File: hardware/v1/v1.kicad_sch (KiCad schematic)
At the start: 70 parts, among them J1 AUDIO IN, J2 MIDI OUT, J3 MIDI IN, J4 MIDI THRU, J5 OUTPUT R, J6 OUTPUT L - MONO, J7 EXP 2, J8 EXP 1, J9 Conn_01x02_Female, SW1 RotaryEncoder_Switch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

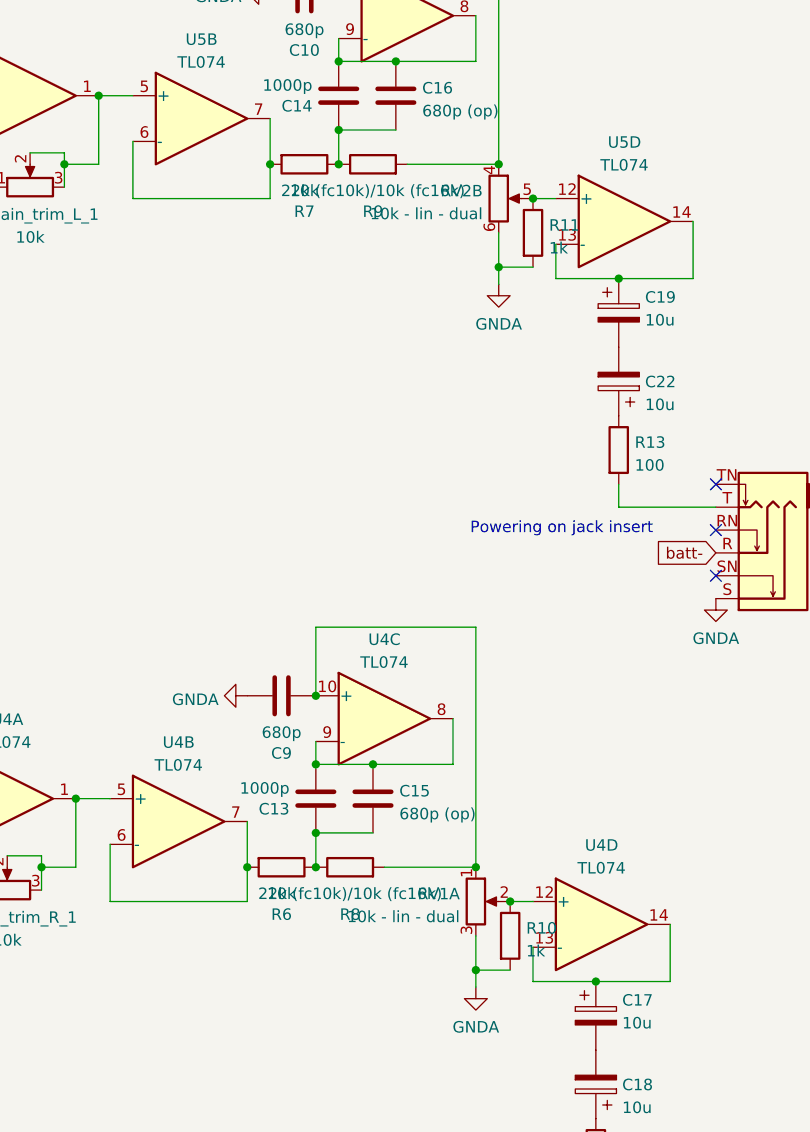
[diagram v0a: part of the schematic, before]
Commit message: Added DIN5 Midi component
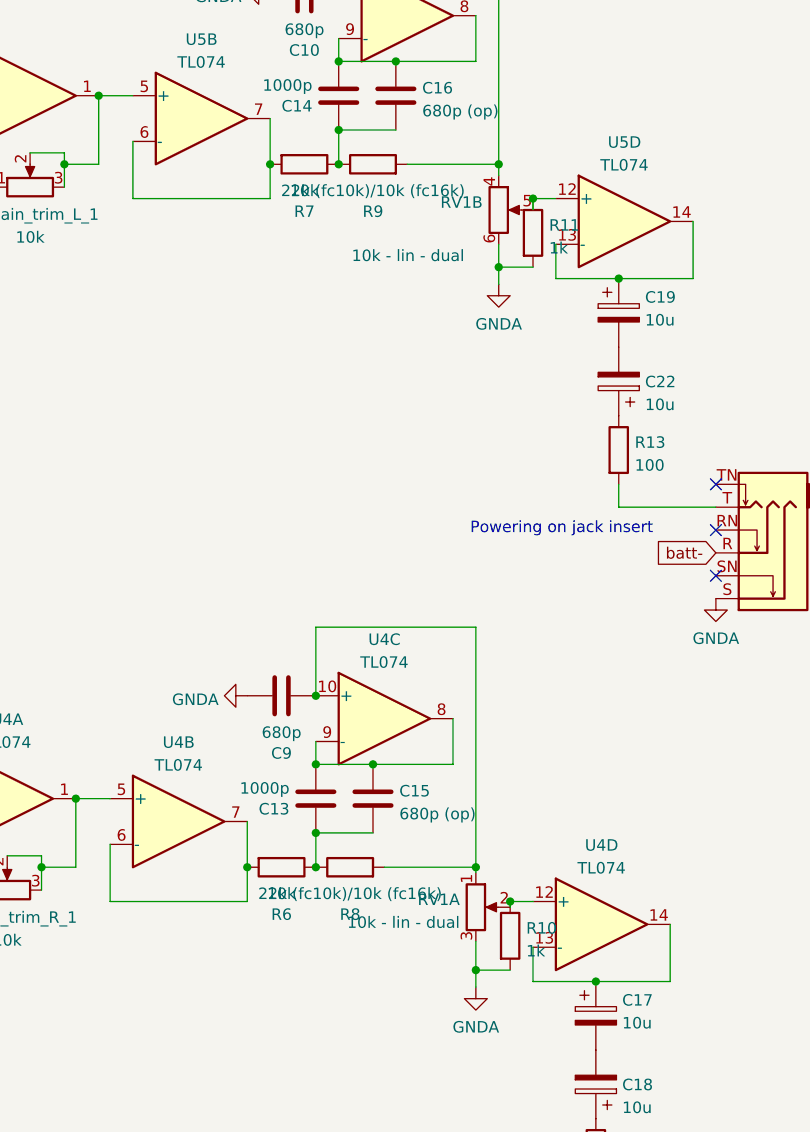
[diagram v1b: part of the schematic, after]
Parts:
- J2, J3, J4: footprint (none) -> MIDI_DIN5:DS-5 MIDI
- renumbered RV2 to RV1
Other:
- moved on the sheet: RV1A, RV1B
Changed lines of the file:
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@@
     (stroke (width 0) (type default) (color 0 0 0 0))
   )
+  (wire (pts (xy 441.96 125.73) (xy 441.96 125.095))
+    (stroke (width 0) (type default) (color 0 0 0 0))
+  )
   (wire (pts (xy 58.42 36.83) (xy 58.42 82.55))
     (stroke (width 0) (type default) (color 0 0 0 0))
@@
     (stroke (width 0) (type default) (color 0 0 0 0))
   )
+  (wire (pts (xy 445.77 129.54) (xy 445.77 128.905))
+    (stroke (width 0) (type default) (color 0 0 0 0))
+  )
   (wire (pts (xy 424.18 111.125) (xy 424.18 113.665))
     (stroke (width 0) (type default) (color 0 0 0 0))
@@
     (stroke (width 0) (type default) (color 0 0 0 0))
   )
-  (wire (pts (xy 441.96 136.525) (xy 441.96 132.715))
+  (wire (pts (xy 441.96 136.525) (xy 441.96 133.35))
     (stroke (width 0) (type default) (color 0 0 0 0))
   )
@@
     (stroke (width 0) (type default) (color 0 0 0 0))
   )
+  (wire (pts (xy 448.31 52.07) (xy 448.31 50.8))
+    (stroke (width 0) (type default) (color 0 0 0 0))
+  )
   (wire (pts (xy 444.5 60.325) (xy 444.5 58.42))
     (stroke (width 0) (type default) (color 0 0 0 0))
@@
     (stroke (width 0) (type default) (color 0 0 0 0))
   )
+  (wire (pts (xy 444.5 48.26) (xy 444.5 46.99))
+    (stroke (width 0) (type default) (color 0 0 0 0))
+  )
   (wire (pts (xy 457.835 82.55) (xy 457.835 85.09))
     (stroke (width 0) (type default) (color 0 0 0 0))
@@
     (stroke (width 0) (type default) (color 0 0 0 0))
   )
-  (wire (pts (xy 444.5 58.42) (xy 444.5 54.61))
+  (wire (pts (xy 444.5 58.42) (xy 444.5 55.88))
     (stroke (width 0) (type default) (color 0 0 0 0))
   )
@@
     (pin "4")
   )
-  (symbol (lib_id "Device:R_Potentiometer_Dual_Separate") (at 441.96 128.905 0) (unit 1)
+  (symbol (lib_id "Device:R_Potentiometer_Dual_Separate") (at 441.96 129.54 0) (unit 1)
     (in_bom yes) (on_board yes) (fields_autoplaced)
-    (property "Reference" "RV1" (id 0) (at 440.182 128.0703 0)
+    (property "Reference" "RV1" (id 0) (at 440.182 128.7053 0)
       (effects (font (size 1.27 1.27)) (justify right))
     )
-    (property "Value" "10k - lin - dual" (id 1) (at 440.182 130.6072 0)
+    (property "Value" "10k - lin - dual" (id 1) (at 440.182 131.2422 0)
       (effects (font (size 1.27 1.27)) (justify right))
     )
-    (property "Footprint" "" (id 2) (at 441.96 128.905 0)
+    (property "Footprint" "" (id 2) (at 441.96 129.54 0)
       (effects (font (size 1.27 1.27)) hide)
     )
-    (property "Datasheet" "~" (id 3) (at 441.96 128.905 0)
+    (property "Datasheet" "~" (id 3) (at 441.96 129.54 0)
       (effects (font (size 1.27 1.27)) hide)
     )
@@
     (property "Reference" "J4" (id 0) (at 263.5251 123.3002 0))
     (property "Value" "MIDI THRU" (id 1) (at 263.5251 125.8371 0))
-    (property "Footprint" "" (id 2) (at 263.525 132.08 0)
+    (property "Footprint" "MIDI_DIN5:DS-5 MIDI" (id 2) (at 263.525 132.08 0)
       (effects (font (size 1.27 1.27)) hide)
     )
@@
       (effects (font (size 1.27 1.27)) (justify right))
     )
-    (property "Footprint" "" (id 2) (at 243.205 132.715 0)
+    (property "Footprint" "MIDI_DIN5:DS-5 MIDI" (id 2) (at 243.205 132.715 0)
       (effects (font (size 1.27 1.27)) hide)
     )
@@
     (property "Reference" "J2" (id 0) (at 167.0051 124.5702 0))
     (property "Value" "MIDI OUT" (id 1) (at 167.0051 127.1071 0))
-    (property "Footprint" "" (id 2) (at 167.005 133.35 0)
+    (property "Footprint" "MIDI_DIN5:DS-5 MIDI" (id 2) (at 167.005 133.35 0)
       (effects (font (size 1.27 1.27)) hide)
     )
@@
     (pin "4")
   )
-  (symbol (lib_id "Device:R_Potentiometer_Dual_Separate") (at 444.5 50.8 0) (unit 2)
-    (in_bom yes) (on_board yes) (fields_autoplaced)
-    (property "Reference" "RV2" (id 0) (at 442.722 49.9653 0)
+  (symbol (lib_id "Device:R_Potentiometer_Dual_Separate") (at 444.5 52.07 0) (unit 2)
+    (in_bom yes) (on_board yes)
+    (property "Reference" "RV1" (id 0) (at 442.722 51.2353 0)
       (effects (font (size 1.27 1.27)) (justify right))
     )
-    (property "Value" "10k - lin - dual" (id 1) (at 442.722 52.5022 0)
+    (property "Value" "10k - lin - dual" (id 1) (at 440.69 57.15 0)
       (effects (font (size 1.27 1.27)) (justify right))
     )
-    (property "Footprint" "" (id 2) (at 444.5 50.8 0)
+    (property "Footprint" "" (id 2) (at 444.5 52.07 0)
       (effects (font (size 1.27 1.27)) hide)
     )
-    (property "Datasheet" "~" (id 3) (at 444.5 50.8 0)
+    (property "Datasheet" "~" (id 3) (at 444.5 52.07 0)
       (effects (font (size 1.27 1.27)) hide)
     )
@@
     )
     (path "/be3f2217-99de-4549-8d21-5a87292252e5"
-      (reference "J2") (unit 1) (value "MIDI OUT") (footprint "")
+      (reference "J2") (unit 1) (value "MIDI OUT") (footprint "MIDI_DIN5:DS-5 MIDI")
     )
     (path "/b1c96566-7940-49f4-a60d-f8a08bd036b1"
-      (reference "J3") (unit 1) (value "MIDI IN") (footprint "")
+      (reference "J3") (unit 1) (value "MIDI IN") (footprint "MIDI_DIN5:DS-5 MIDI")
     )
     (path "/49f76ca1-b75f-49b9-80bf-0c4c4ec1f0ea"
-      (reference "J4") (unit 1) (value "MIDI THRU") (footprint "")
+      (reference "J4") (unit 1) (value "MIDI THRU") (footprint "MIDI_DIN5:DS-5 MIDI")
     )
     (path "/eb1dfd55-7b3f-4e09-9fb1-847ee4ae89e1"
@@
     )
     (path "/c0f91244-7785-4f67-800f-3775e839ff20"
-      (reference "RV2") (unit 2) (value "10k - lin - dual") (footprint "")
+      (reference "RV1") (unit 2) (value "10k - lin - dual") (footprint "")
     )
     (path "/d7195655-bc8b-42c6-9265-3feac398262b"

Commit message: Added stamp dual pot
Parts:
- RV1: footprint (none) -> dual_pot:Dual Pot RK1114GH
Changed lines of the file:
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@@
       (effects (font (size 1.27 1.27)) (justify right))
     )
-    (property "Footprint" "" (id 2) (at 441.96 129.54 0)
+    (property "Footprint" "dual_pot:Dual Pot RK1114GH" (id 2) (at 441.96 129.54 0)
       (effects (font (size 1.27 1.27)) hide)
     )
@@
       (effects (font (size 1.27 1.27)) (justify right))
     )
-    (property "Footprint" "" (id 2) (at 444.5 52.07 0)
+    (property "Footprint" "dual_pot:Dual Pot RK1114GH" (id 2) (at 444.5 52.07 0)
       (effects (font (size 1.27 1.27)) hide)
     )
@@
     )
     (path "/1dbdedeb-a12d-4a03-88a7-8dc9f8b82f58"
-      (reference "RV1") (unit 1) (value "10k - lin - dual") (footprint "")
+      (reference "RV1") (unit 1) (value "10k - lin - dual") (footprint "dual_pot:Dual Pot RK1114GH")
     )
     (path "/c0f91244-7785-4f67-800f-3775e839ff20"
-      (reference "RV1") (unit 2) (value "10k - lin - dual") (footprint "")
+      (reference "RV1") (unit 2) (value "10k - lin - dual") (footprint "dual_pot:Dual Pot RK1114GH")
     )
     (path "/d7195655-bc8b-42c6-9265-3feac398262b"

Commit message: Added screen stamp
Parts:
- U3: footprint (none) -> TFT_Screens:TFT_2.4
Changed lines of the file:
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@@
     (property "Reference" "U3" (id 0) (at 178.435 66.201 0))
     (property "Value" "2.4inches" (id 1) (at 178.435 68.7379 0))
-    (property "Footprint" "" (id 2) (at 180.975 82.55 0)
+    (property "Footprint" "TFT_Screens:TFT_2.4" (id 2) (at 180.975 82.55 0)
       (effects (font (size 1.27 1.27)) hide)
     )
@@
     )
     (path "/bc33b228-85e6-4d5d-99b9-88d2a0d93ad5"
-      (reference "U3") (unit 1) (value "2.4inches") (footprint "")
+      (reference "U3") (unit 1) (value "2.4inches") (footprint "TFT_Screens:TFT_2.4")
     )
     (path "/4e48de9c-53a5-47eb-ae60-7f5ccb2d118e"

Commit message: started pcb
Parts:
- U1: footprint Housings_SOIC:SOIC-8_3.9x4.9mm_Pitch1.27mm -> Package_SO:SOP-8_3.9x4.9mm_P1.27mm
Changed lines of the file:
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@@
     (property "Reference" "U1" (id 0) (at 83.82 26.7802 0))
     (property "Value" "PT8211-pt8211" (id 1) (at 83.82 29.3171 0))
-    (property "Footprint" "Housings_SOIC:SOIC-8_3.9x4.9mm_Pitch1.27mm" (id 2) (at 83.82 39.37 0)
+    (property "Footprint" "Package_SO:SOP-8_3.9x4.9mm_P1.27mm" (id 2) (at 83.82 39.37 0)
       (effects (font (size 1.27 1.27) italic) hide)
     )
@@
     )
     (path "/55be732d-d054-4d1b-b915-371f3d6eb5d0"
-      (reference "U1") (unit 1) (value "PT8211-pt8211") (footprint "Housings_SOIC:SOIC-8_3.9x4.9mm_Pitch1.27mm")
+      (reference "U1") (unit 1) (value "PT8211-pt8211") (footprint "Package_SO:SOP-8_3.9x4.9mm_P1.27mm")
     )
     (path "/98f5bc82-3b1e-4f7c-9aea-552da5d9b877"

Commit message: started PCB
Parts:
- J9: footprint Connector_JST:JST_XH_B2B-XH-AM_1x02_P2.50mm_Vertical -> Connector_JST:JST_XH_B2B-XH-A_1x02_P2.50mm_Vertical
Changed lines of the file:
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@@
       (effects (font (size 1.27 1.27)) (justify left))
     )
-    (property "Footprint" "Connector_JST:JST_XH_B2B-XH-AM_1x02_P2.50mm_Vertical" (id 2) (at 249.555 26.035 0)
+    (property "Footprint" "Connector_JST:JST_XH_B2B-XH-A_1x02_P2.50mm_Vertical" (id 2) (at 249.555 26.035 0)
       (effects (font (size 1.27 1.27)) hide)
     )
@@
     )
     (path "/3ed761fc-73b0-4fad-9c40-d3c2aa5128e2"
-      (reference "J9") (unit 1) (value "Conn_01x02_Female") (footprint "Connector_JST:JST_XH_B2B-XH-AM_1x02_P2.50mm_Vertical")
+      (reference "J9") (unit 1) (value "Conn_01x02_Female") (footprint "Connector_JST:JST_XH_B2B-XH-A_1x02_P2.50mm_Vertical")
     )
     (path "/7aa8ebeb-8bea-4614-8ec6-7c790f165918"

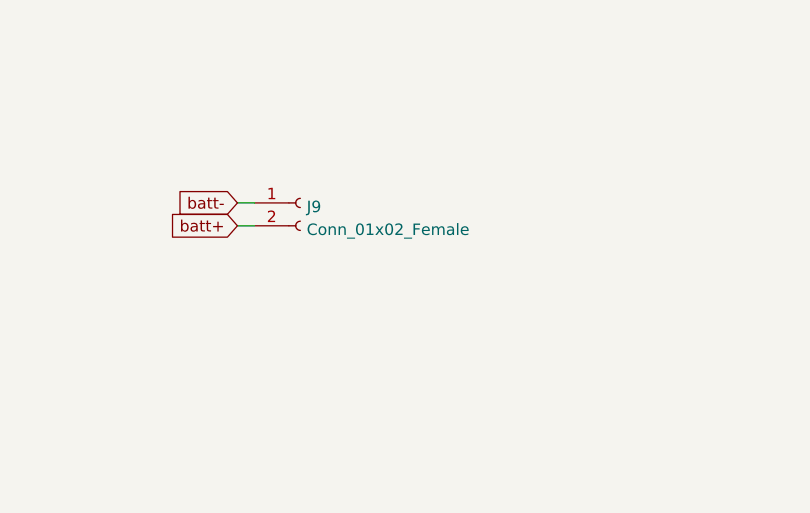
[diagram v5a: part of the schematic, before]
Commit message: Continued PCB placing
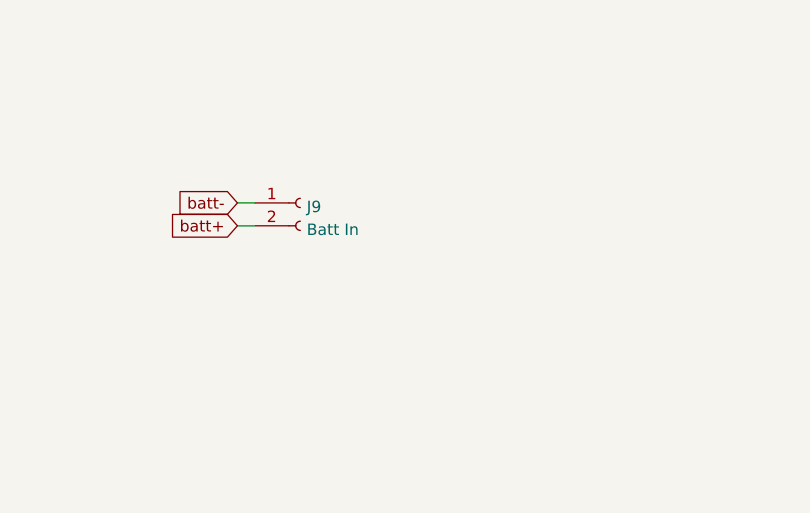
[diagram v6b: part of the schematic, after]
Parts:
- J9: value Conn_01x02_Female -> Batt In
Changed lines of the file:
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@@
       (effects (font (size 1.27 1.27)) (justify left))
     )
-    (property "Value" "Conn_01x02_Female" (id 1) (at 250.2662 29.0072 0)
+    (property "Value" "Batt In" (id 1) (at 250.2662 29.0072 0)
       (effects (font (size 1.27 1.27)) (justify left))
     )
@@
     )
     (path "/3ed761fc-73b0-4fad-9c40-d3c2aa5128e2"
-      (reference "J9") (unit 1) (value "Conn_01x02_Female") (footprint "Connector_JST:JST_XH_B2B-XH-A_1x02_P2.50mm_Vertical")
+      (reference "J9") (unit 1) (value "Batt In") (footprint "Connector_JST:JST_XH_B2B-XH-A_1x02_P2.50mm_Vertical")
     )
     (path "/7aa8ebeb-8bea-4614-8ec6-7c790f165918"

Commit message: Added header for battery or USB powering
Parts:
- added J10: Close for battery power, Connector_PinHeader_2.54mm:PinHeader_1x02_P2.54mm_Vertical, symbol Connector:Conn_01x02_Male
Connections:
- net batt-: now also J10.1 (Pin_1); no longer J6.R
- new net: J10.2 (Pin_2), J6.R
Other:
- note added: "Powering on jack insert Can be disabled by opening the header for avoiding shorts during programmation"
- note removed: "Powering on jack insert"
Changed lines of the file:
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@@
     (stroke (width 0) (type default) (color 0 0 0 0))
   )
-  (wire (pts (xy 57.15 113.03) (xy 66.04 113.03))
+  (wire (pts (xy 50.165 113.03) (xy 66.04 113.03))
     (stroke (width 0) (type default) (color 0 0 0 0))
   )
@@
     (stroke (width 0) (type default) (color 0 0 0 0))
   )
+  (wire (pts (xy 442.595 90.17) (xy 456.565 90.17))
+    (stroke (width 0) (type default) (color 0 0 0 0))
+  )
   (wire (pts (xy 107.95 92.71) (xy 107.95 87.63))
     (stroke (width 0) (type default) (color 0 0 0 0))
@@
     (stroke (width 0) (type default) (color 0 0 0 0))
   )
+  (wire (pts (xy 54.61 105.41) (xy 66.04 105.41))
+    (stroke (width 0) (type default) (color 0 0 0 0))
+  )
   (wire (pts (xy 153.67 15.24) (xy 163.195 15.24))
     (stroke (width 0) (type default) (color 0 0 0 0))
@@
   )
   (wire (pts (xy 198.755 90.17) (xy 197.485 90.17))
+    (stroke (width 0) (type default) (color 0 0 0 0))
+  )
+  (wire (pts (xy 459.105 90.17) (xy 468.63 90.17))
     (stroke (width 0) (type default) (color 0 0 0 0))
   )
@@
     (effects (font (size 1.27 1.27)) (justify left bottom))
   )
-  (text "Powering on jack insert" (at 441.325 88.265 0)
+  (text "Powering on jack insert\nCan be disabled by opening the header\nfor avoiding shorts during programmation"
+    (at 415.925 87.63 0)
     (effects (font (size 1.27 1.27)) (justify left bottom))
   )
@@
     )
   )
-  (global_label "batt-" (shape input) (at 468.63 90.17 180) (fields_autoplaced)
+  (global_label "batt-" (shape input) (at 442.595 90.17 180) (fields_autoplaced)
     (effects (font (size 1.27 1.27)) (justify right))
-    (property "Références Inter-Feuilles" "${INTERSHEET_REFS}" (id 0) (at 460.895 90.0906 0)
+    (property "Références Inter-Feuilles" "${INTERSHEET_REFS}" (id 0) (at 434.86 90.0906 0)
       (effects (font (size 1.27 1.27)) (justify right) hide)
     )
@@
     )
   )
-  (global_label "batt+" (shape input) (at 57.15 113.03 180) (fields_autoplaced)
+  (global_label "batt+" (shape input) (at 50.165 113.03 180) (fields_autoplaced)
     (effects (font (size 1.27 1.27)) (justify right))
-    (property "Références Inter-Feuilles" "${INTERSHEET_REFS}" (id 0) (at 49.415 112.9506 0)
+    (property "Références Inter-Feuilles" "${INTERSHEET_REFS}" (id 0) (at 42.43 112.9506 0)
       (effects (font (size 1.27 1.27)) (justify right) hide)
     )
@@
     (pin "11")
     (pin "4")
+  )
+  (symbol (lib_id "Connector:Conn_01x02_Male") (at 456.565 95.25 90) (unit 1)
+    (in_bom yes) (on_board yes) (fields_autoplaced)
+    (property "Reference" "J10" (id 0) (at 459.9432 93.7803 90)
+      (effects (font (size 1.27 1.27)) (justify right))
+    )
+    (property "Value" "Close for battery power" (id 1) (at 459.9432 96.3172 90)
+      (effects (font (size 1.27 1.27)) (justify right))
+    )
+    (property "Footprint" "Connector_PinHeader_2.54mm:PinHeader_1x02_P2.54mm_Vertical" (id 2) (at 456.565 95.25 0)
+      (effects (font (size 1.27 1.27)) hide)
+    )
+    (property "Datasheet" "~" (id 3) (at 456.565 95.25 0)
+      (effects (font (size 1.27 1.27)) hide)
+    )
+    (pin "1")
+    (pin "2")
   )
   (symbol (lib_id "power:GNDA") (at 43.815 145.415 90) (unit 1)
@@
     (pin "5")
   )
-  (symbol (lib_id "power:+3V3") (at 66.04 105.41 90) (unit 1)
-    (in_bom yes) (on_board yes) (fields_autoplaced)
-    (property "Reference" "#PWR02" (id 0) (at 69.85 105.41 0)
-      (effects (font (size 1.27 1.27)) hide)
-    )
-    (property "Value" "+3V3" (id 1) (at 62.865 105.8438 90)
-      (effects (font (size 1.27 1.27)) (justify left))
-    )
-    (property "Footprint" "" (id 2) (at 66.04 105.41 0)
-      (effects (font (size 1.27 1.27)) hide)
-    )
-    (property "Datasheet" "" (id 3) (at 66.04 105.41 0)
+  (symbol (lib_id "power:+3V3") (at 54.61 105.41 90) (unit 1)
+    (in_bom yes) (on_board yes) (fields_autoplaced)
+    (property "Reference" "#PWR02" (id 0) (at 58.42 105.41 0)
+      (effects (font (size 1.27 1.27)) hide)
+    )
+    (property "Value" "+3V3" (id 1) (at 51.435 105.8438 90)
+      (effects (font (size 1.27 1.27)) (justify left))
+    )
+    (property "Footprint" "" (id 2) (at 54.61 105.41 0)
+      (effects (font (size 1.27 1.27)) hide)
+    )
+    (property "Datasheet" "" (id 3) (at 54.61 105.41 0)
       (effects (font (size 1.27 1.27)) hide)
     )
@@
       (reference "J9") (unit 1) (value "Batt In") (footprint "Connector_JST:JST_XH_B2B-XH-A_1x02_P2.50mm_Vertical")
     )
+    (path "/72a3182d-52e3-4382-976b-73291daa2ea7"
+      (reference "J10") (unit 1) (value "Close for battery power") (footprint "Connector_PinHeader_2.54mm:PinHeader_1x02_P2.54mm_Vertical")
+    )
     (path "/7aa8ebeb-8bea-4614-8ec6-7c790f165918"
